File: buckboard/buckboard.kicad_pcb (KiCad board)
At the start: 2 copper layers, 171.4 x 100.4 mm, 0 parts

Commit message: Buckboard Beta 1
Ready for Ochoa review
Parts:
- added REF**: PinHeader_2x06_P2.54mm_Vertical, Connector_PinHeader_2.54mm:PinHeader_2x06_P2.54mm_Vertical, F.Cu at (213.8, 73.8)
- added REF**: MountingHole_2.2mm_M2, MountingHole:MountingHole_2.2mm_M2, F.Cu at (230.6, 72.8)
- added REF**: PinHeader_1x02_P2.54mm_Vertical, Connector_PinHeader_2.54mm:PinHeader_1x02_P2.54mm_Vertical, F.Cu at (216.3, 85.8)
- added REF**: MountingHole_2.2mm_M2, MountingHole:MountingHole_2.2mm_M2, F.Cu at (181.6, 72.8)
- added REF**: MountingHole_2.2mm_M2, MountingHole:MountingHole_2.2mm_M2, F.Cu at (174.9, 56.0)
- added REF**: PinHeader_1x02_P2.54mm_Vertical, Connector_PinHeader_2.54mm:PinHeader_1x02_P2.54mm_Vertical, F.Cu at (104.6, 103.4)
- added REF**: MountingHole_2.2mm_M2, MountingHole:MountingHole_2.2mm_M2, F.Cu at (118.9, 93.9)
- added REF**: MountingHole_2.2mm_M2, MountingHole:MountingHole_2.2mm_M2, F.Cu at (209.6, 72.8)
- added REF**: MountingHole_3.2mm_M3, MountingHole:MountingHole_3.2mm_M3, F.Cu at (231.1, 80.7)
- added REF**: MountingHole_2.2mm_M2, MountingHole:MountingHole_2.2mm_M2, F.Cu at (153.9, 72.7)
- added REF**: PinHeader_1x02_P2.54mm_Vertical, Connector_PinHeader_2.54mm:PinHeader_1x02_P2.54mm_Vertical, F.Cu at (160.6, 95.1)
- added REF**: PinHeader_2x06_P2.54mm_Vertical, Connector_PinHeader_2.54mm:PinHeader_2x06_P2.54mm_Vertical, F.Cu at (185.8, 73.8)
- added REF**: MountingHole_2.2mm_M2, MountingHole:MountingHole_2.2mm_M2, F.Cu at (202.6, 56.1)
- added REF**: MountingHole_2.2mm_M2, MountingHole:MountingHole_2.2mm_M2, F.Cu at (202.6, 72.8)
- added REF**: MountingHole_2.2mm_M2, MountingHole:MountingHole_2.2mm_M2, F.Cu at (230.6, 56.1)
- added REF**: MountingHole_2.2mm_M2, MountingHole:MountingHole_2.2mm_M2, F.Cu at (125.9, 83.4)
- added REF**: Samtec_HPM-02-01-x-S_Straight_1x02_Pitch5.08mm, Connector_Samtec_HPM_THT:Samtec_HPM-02-01-x-S_Straight_1x02_Pitch5.08mm, F.Cu at (84.1, 82.4)
- added REF**: MountingHole_2.2mm_M2, MountingHole:MountingHole_2.2mm_M2, F.Cu at (118.9, 77.2)
- added REF**: PinHeader_2x06_P2.54mm_Vertical, Connector_PinHeader_2.54mm:PinHeader_2x06_P2.54mm_Vertical, F.Cu at (102.0, 94.8)
- added REF**: PinHeader_2x06_P2.54mm_Vertical, Connector_PinHeader_2.54mm:PinHeader_2x06_P2.54mm_Vertical, F.Cu at (130.0, 84.4)
- added REF**: MountingHole_3.2mm_M3, MountingHole:MountingHole_3.2mm_M3, F.Cu at (105.5, 110.3)
- added REF**: PinHeader_2x06_P2.54mm_Vertical, Connector_PinHeader_2.54mm:PinHeader_2x06_P2.54mm_Vertical, F.Cu at (158.0, 73.6)
- added REF**: MountingHole_2.2mm_M2, MountingHole:MountingHole_2.2mm_M2, F.Cu at (146.8, 66.7)
- added REF**: PinHeader_1x02_P2.54mm_Vertical, Connector_PinHeader_2.54mm:PinHeader_1x02_P2.54mm_Vertical, F.Cu at (132.5, 100.3)
- added REF**: PinHeader_1x02_P2.54mm_Vertical, Connector_PinHeader_2.54mm:PinHeader_1x02_P2.54mm_Vertical, F.Cu at (188.3, 90.9)
- added REF**: MountingHole_3.2mm_M3, MountingHole:MountingHole_3.2mm_M3, F.Cu at (98.6, 70.8)
- added REF**: MountingHole_2.2mm_M2, MountingHole:MountingHole_2.2mm_M2, F.Cu at (146.8, 83.4)
- added REF**: MountingHole_2.2mm_M2, MountingHole:MountingHole_2.2mm_M2, F.Cu at (174.9, 72.7)
- added REF**: MountingHole_2.2mm_M2, MountingHole:MountingHole_2.2mm_M2, F.Cu at (97.9, 93.9)
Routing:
- net VIN: track 0.00 -> 211.2 mm
- net 12V1: track 0.00 -> 24.0 mm
- net 12V2: track 0.00 -> 19.6 mm
- net 9V: track 0.00 -> 18.4 mm
- net 12V3: track 0.00 -> 14.6 mm
- net 5V: track 0.00 -> 11.0 mm
- added copper zone on B.Cu, net GND
- added copper zone on F.Cu, net GND
- added copper zone on B.Cu, net VIN
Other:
- board size 171.4 x 100.4 mm -> 164.2 x 68.1 mm
- board text added: "+"
- board text added: "-"
- board text added: "12V1"
- board text added: "12V2"
- board text added: "12V3"
- board text removed: "12V(1)"
- board text removed: "12V(2)"
- board text removed: "12V(3)"
- board text removed: "3V"

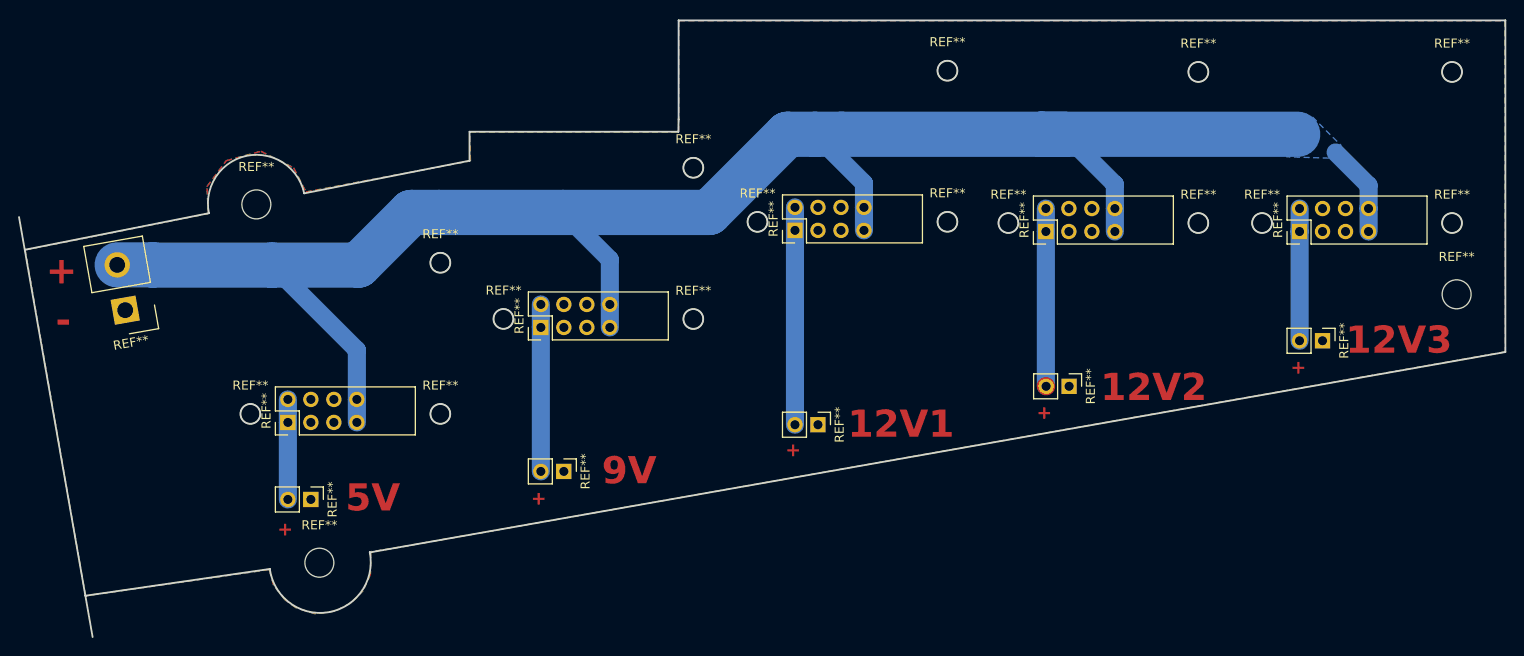
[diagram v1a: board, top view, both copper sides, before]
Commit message: Displayboard added
V1 of displayboard, this includes the SSD1309 and EC11 Rotary encoder with 1x04 JST connectors at 2.5mm pitch
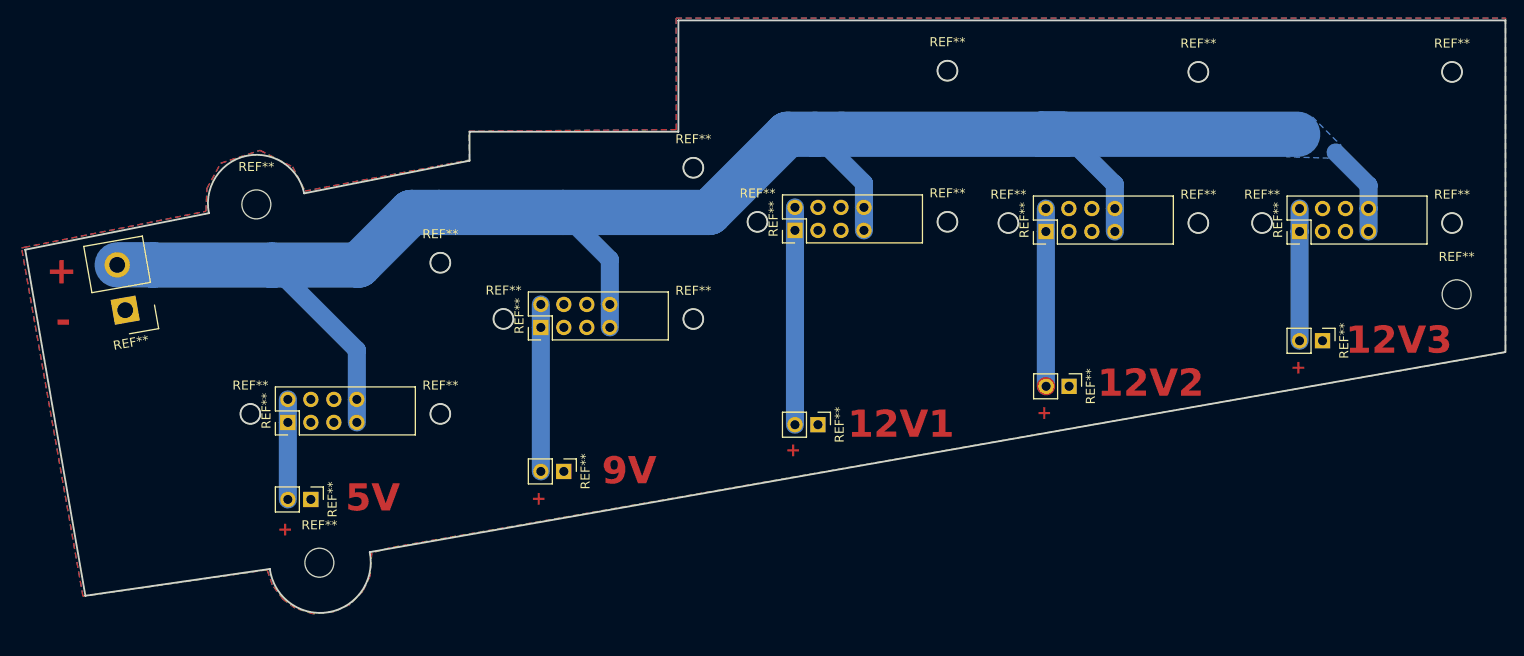
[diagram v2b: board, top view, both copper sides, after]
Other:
- board size 164.2 x 68.1 mm -> 163.5 x 65.4 mm
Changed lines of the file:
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@@
 	)
 	(setup
+		(stackup
+			(layer "F.SilkS"
+				(type "Top Silk Screen")
+			)
+			(layer "F.Paste"
+				(type "Top Solder Paste")
+			)
+			(layer "F.Mask"
+				(type "Top Solder Mask")
+				(thickness 0.01)
+			)
+			(layer "F.Cu"
+				(type "copper")
+				(thickness 0.035)
+			)
+			(layer "dielectric 1"
+				(type "core")
+				(thickness 1.51)
+				(material "FR4")
+				(epsilon_r 4.5)
+				(loss_tangent 0.02)
+			)
+			(layer "B.Cu"
+				(type "copper")
+				(thickness 0.035)
+			)
+			(layer "B.Mask"
+				(type "Bottom Solder Mask")
+				(thickness 0.01)
+			)
+			(layer "B.Paste"
+				(type "Bottom Solder Paste")
+			)
+			(layer "B.SilkS"
+				(type "Bottom Silk Screen")
+			)
+			(copper_finish "None")
+			(dielectric_constraints no)
+		)
 		(pad_to_mask_clearance 0)
 		(allow_soldermask_bridges_in_footprints no)
@@
 		(layer "Dwgs.User")
 	)
+	(gr_circle
+		(center 231.14 80.6958)
+		(end 231.7242 79.248)
+		(stroke
+			(width 0.1)
+			(type default)
+		)
+		(fill no)
+		(layer "Dwgs.User")
+	)
 	(gr_line
 		(start 198.625855 32.258)
@@
 	)
 	(gr_line
+		(start 72.9996 75.7682)
+		(end 79.6544 114.0206)
+		(stroke
+			(width 0.1)
+			(type default)
+		)
+		(layer "Dwgs.User")
+	)
+	(gr_line
 		(start 79.8576 70.779807)
 		(end 72.253308 72.120649)
@@
 		(layer "Edge.Cuts")
 	)
-	(gr_line
-		(start 80.4672 118.5418)
-		(end 72.3392 72.1614)
-		(stroke
-			(width 0.2)
-			(type default)
-		)
-		(layer "Edge.Cuts")
-	)
 	(gr_circle
 		(center 181.61 72.8218)
@@
 	)
 	(gr_line
+		(start 236.4994 87.0712)
+		(end 111.074199 109.1692)
+		(stroke
+			(width 0.2)
+			(type default)
+		)
+		(layer "Edge.Cuts")
+	)
+	(gr_line
 		(start 73.025 75.7682)
 		(end 93.310391 71.736164)
@@
 		(layer "Edge.Cuts")
 	)
+	(gr_line
+		(start 236.4994 50.4444)
+		(end 236.4994 87.0712)
+		(stroke
+			(width 0.2)
+			(type default)
+		)
+		(layer "Edge.Cuts")
+	)
 	(gr_arc
 		(start 111.0742 109.1692)
@@
 	)
 	(gr_line
-		(start 145.1864 50.4444)
-		(end 145.1864 61.3664)
-		(stroke
-			(width 0.2)
-			(type default)
-		)
-		(layer "Edge.Cuts")
-	)
-	(gr_line
 		(start 122.0978 65.9384)
 		(end 122.0978 62.738)
@@
 		(layer "Edge.Cuts")
 	)
-	(gr_line
-		(start 145.1864 50.4444)
-		(end 236.4994 50.4444)
-		(stroke
-			(width 0.2)
-			(type default)
-		)
-		(layer "Edge.Cuts")
-	)
 	(gr_circle
 		(center 230.6066 72.8218)
@@
 		(layer "Edge.Cuts")
 	)
-	(gr_circle
-		(center 174.879 56.007)
-		(end 174.1678 56.8452)
+	(gr_line
+		(start 145.161 62.738)
+		(end 145.161 50.4444)
 		(stroke
 			(width 0.2)
 			(type default)
 		)
-		(fill no)
 		(layer "Edge.Cuts")
 	)
-	(gr_line
-		(start 122.0978 62.738)
-		(end 145.161 62.738)
+	(gr_circle
+		(center 174.879 56.007)
+		(end 174.1678 56.8452)
 		(stroke
 			(width 0.2)
 			(type default)
 		)
+		(fill no)
 		(layer "Edge.Cuts")
 	)
@@
 		(layer "Edge.Cuts")
 	)
-	(gr_line
-		(start 236.4994 50.4444)
-		(end 236.4994 87.0712)
-		(stroke
-			(width 0.2)
-			(type default)
-		)
-		(layer "Edge.Cuts")
-	)
 	(gr_circle
 		(center 97.8916 93.9038)
@@
 		(layer "Edge.Cuts")
 	)
-	(gr_line
-		(start 111.08114 109.203835)
-		(end 236.4994 87.0712)
-		(stroke
-			(width 0.2)
-			(type default)
-		)
-		(layer "Edge.Cuts")
-	)
 	(gr_circle
 		(center 146.812 66.7258)
@@
 		(layer "Edge.Cuts")
 	)
+	(gr_circle
+		(center 230.6066 56.134)
+		(end 229.8954 56.9722)
+		(stroke
+			(width 0.2)
+			(type default)
+		)
+		(fill no)
+		(layer "Edge.Cuts")
+	)
 	(gr_line
-		(start 145.161 62.738)
-		(end 145.1864 61.3664)
+		(start 79.669096 113.98762)
+		(end 73.025 75.7682)
 		(stroke
 			(width 0.2)
@@
 		(layer "Edge.Cuts")
 	)
-	(gr_circle
-		(center 230.6066 56.134)
-		(end 229.8954 56.9722)
+	(gr_line
+		(start 122.0978 62.738)
+		(end 145.161 62.738)
 		(stroke
 			(width 0.2)
 			(type default)
 		)
-		(fill no)
 		(layer "Edge.Cuts")
 	)
@@
 		(layer "Edge.Cuts")
 	)
+	(gr_line
+		(start 145.161 50.4444)
+		(end 236.4994 50.4444)
+		(stroke
+			(width 0.2)
+			(type default)
+		)
+		(layer "Edge.Cuts")
+	)
 	(gr_text "12V1"
 		(at 163.8554 96.7994 0)
@@
 	)
 	(gr_text "12V2"
-		(at 191.77 92.7354 0)
+		(at 191.4398 92.2528 0)
 		(layer "F.Cu")
 		(effects
@@
 		(polygon
 			(pts
-				(xy 73.025 75.7936) (xy 93.2434 71.7804) (xy 93.091 68.8086) (xy 95.2246 65.9384) (xy 99.06 64.897)
-				(xy 102.6668 66.7258) (xy 104.0384 69.3928) (xy 122.1994 65.9638) (xy 122.1232 62.7888) (xy 145.1864 62.7888)
-				(xy 145.2118 50.4698) (xy 236.4486 50.4698) (xy 236.4994 87.0458) (xy 113.4364 108.7882) (xy 111.2012 109.1184)
-				(xy 111.1504 111.633) (xy 110.3376 113.4364) (xy 109.0168 114.7826) (xy 107.2134 115.697) (xy 105.029 115.9764)
-				(xy 102.9716 115.3414) (xy 101.7016 114.427) (xy 100.457 112.8268) (xy 99.9744 111.0996) (xy 79.6798 113.9952)
-				(xy 73.025 75.8444)
+				(xy 72.9234 75.5142) (xy 92.9894 71.5264) (xy 93.091 69.0118) (xy 94.615 66.2178) (xy 98.9584 64.7954)
+				(xy 102.5652 66.6242) (xy 103.9368 69.2912) (xy 122.0978 65.8622) (xy 122.0216 62.6872) (xy 144.9324 62.5094)
+				(xy 144.907 50.1904) (xy 236.5248 50.1904) (xy 236.5248 87.0966) (xy 113.3348 108.6866) (xy 111.3028 109.2454)
+				(xy 111.0996 111.8362) (xy 110.3122 113.4872) (xy 108.9152 114.935) (xy 107.1372 115.7478) (xy 104.8004 115.9764)
+				(xy 102.8192 115.3414) (xy 101.4984 114.3762) (xy 100.3046 112.776) (xy 99.7458 111.125) (xy 79.4004 114.046)
+				(xy 72.6186 75.565)
 			)
 		)
@@
 		)
 	)
+	(group ""
+		(members "08ac290c-cd75-446d-a283-69a62430721d" "100f6bb0-8ac1-4aa8-8df4-68425ee58a96"
+			"14fcc44f-f9c8-4de5-a443-d8060994849b" "19a24748-5a23-4def-b4ac-534d46091593"
+			"1f5220b4-85c4-4825-9cb8-5540edd776f1" "29a9c7e6-edba-41b2-88ba-42d74fc42518"
+			"3b85ee02-43b3-49b5-8263-29d65321620f" "3e021f75-e3d1-466f-a82d-592c27f220af"
+			"487a05c4-4d65-4580-81c5-162e8570d186" "492f5762-d367-4f8f-89e6-e75369b99074"
+			"522a5daa-b4cc-4f55-8a43-47368492fb03" "53abff7b-cace-44b8-a80f-b22d5f4d4c50"
+			"54f060bc-0780-4725-9e6f-3ea997aea16f" "69adb5fd-d910-45b1-b241-f7b099c2820d"
+			"6adc377e-e88e-4b54-bdba-fac3ffd49ba0" "6e200bb5-f3e1-41d2-8d77-5c1d2503f099"
+			"728d0a3e-a5f4-4685-bcae-40d5e5fbf530" "74165322-ee42-419d-bd47-88f6423765a2"
+			"753f1005-65d1-4fc4-b77d-4bd882c4ae62" "7c9931a1-2599-4b11-be92-e460cc33d30c"
+			"7e308f98-fb6c-45fa-b5be-21807d6c1e51" "803e3df1-39b3-4b50-9648-588f74422d63"
+			"86e9b90d-82b7-4cb8-b2d2-05c636e7abfc" "8ab7ee58-7a19-4eaf-a512-e4e011e104a4"
+			"9a4d98c8-8188-4a34-ba1d-e7185f168cd8" "9fdf1d90-d9f6-4e2e-80a1-ef531dc6205f"
+			"a3b4a6e2-f054-4eb3-8551-e894acd52332" "a4385cd8-49ca-4996-aca1-30fc9fb4e0fb"
+			"ad450666-beea-4056-aa28-05f9b408d53b" "ae7e8b20-3739-4d6c-80e1-d8a6fa7bc08d"
+			"ba623425-5180-43ef-b5dc-61c3fc3b580d" "c939d797-44a2-47a3-ba63-0be7c99642f2"
+			"cc096376-f6ec-4625-a543-b02c33cafc7a" "d3aad463-800c-471e-8e0a-56622d526e9b"
+			"d5f47c33-46c5-4eef-8c19-71c94d36bad1" "d92017c2-8270-4b24-a4d1-3dc9bd8df992"
+			"ddb90e7e-b805-409e-8145-4f357c224431" "e011034f-33a2-48b9-9f87-4f56acfee713"
+			"e35176ff-c8aa-4430-be5a-05ac66e4ad7f" "e3cce3ca-6085-4f91-810d-08f08806099e"
+			"e6b83a4e-7aae-4d3d-bdc8-64fd230ead2f" "e8bd8532-d39e-4069-8c25-a64634412c35"
+			"ed3d3a9c-fba3-4353-831f-3840b9a1c39f" "ff6776fd-2066-4b64-a103-c9d81213c82c"
+		)
+	)

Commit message: V1.2
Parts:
- removed the REF** at (146.8, 66.7)
- added REF**: Fuseholder_Cylinder-5x20mm_Schurter_0031_8201_Horizontal_Op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, Fuse:Fuseholder_Cylinder-5x20mm_Schurter_0031_8201_Horizontal_Open, F.Cu at (125.7, 87.8)
- added REF**: Fuseholder_Cylinder-5x20mm_Schurter_0031_8201_Horizontal_Op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, Fuse:Fuseholder_Cylinder-5x20mm_Schurter_0031_8201_Horizontal_Open, F.Cu at (106.9, 87.7)
- added REF**: Fuseholder_Cylinder-5x20mm_Schurter_0031_8201_Horizontal_Op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, Fuse:Fuseholder_Cylinder-5x20mm_Schurter_0031_8201_Horizontal_Open, F.Cu at (175.0, 78.6)
- added REF**: PinHeader_2x06_P2.54mm_Vertical, Connector_PinHeader_2.54mm:PinHeader_2x06_P2.54mm_Vertical, F.Cu at (158.1, 108.7)
- added REF**: PinHeader_1x02_P2.54mm_Vertical, Connector_PinHeader_2.54mm:PinHeader_1x02_P2.54mm_Vertical, F.Cu at (160.8, 113.5)
- added REF**: MountingHole_2.2mm_M2, MountingHole:MountingHole_2.2mm_M2, F.Cu at (175.0, 107.9)
- added REF**: Fuseholder_Cylinder-5x20mm_Schurter_0031_8201_Horizontal_Op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, Fuse:Fuseholder_Cylinder-5x20mm_Schurter_0031_8201_Horizontal_Open, F.Cu at (174.7, 37.5)
- added REF**: MountingHole_2.2mm_M2, MountingHole:MountingHole_2.2mm_M2, F.Cu at (153.9, 107.9)
- added REF**: Fuseholder_Cylinder-5x20mm_Schurter_0031_8201_Horizontal_Op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, Fuse:Fuseholder_Cylinder-5x20mm_Schurter_0031_8201_Horizontal_Open, F.Cu at (193.7, 68.6)
- added REF**: Fuseholder_Cylinder-5x20mm_Schurter_0031_8201_Horizontal_Op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, Fuse:Fuseholder_Cylinder-5x20mm_Schurter_0031_8201_Horizontal_Open, F.Cu at (183.0, 61.8)
- added REF**: MountingHole_2.2mm_M2, MountingHole:MountingHole_2.2mm_M2, F.Cu at (175.0, 86.8)
- moved REF** 61.8 mm to (184.0, 66.1)
- moved REF** 59.1 mm to (113.8, 116.2)
- moved REF** 59.1 mm to (134.9, 116.2)
- moved REF** 59.1 mm to (118.0, 117.0)
- moved REF** 55.9 mm to (134.9, 95.1)
- moved REF** 47.6 mm to (120.6, 121.0)
- moved REF** 32.6 mm to (175.0, 67.1)
- moved REF** 32.6 mm to (158.1, 68.0)
- moved REF** 32.5 mm to (153.9, 67.1)
- moved REF** 29.8 mm to (84.6, 120.5)
- moved REF** 29.7 mm to (105.6, 120.5)
- moved REF** 29.7 mm to (88.8, 121.4)
- moved REF** 26.0 mm to (91.3, 125.6)
- moved REF** 26.0 mm to (105.6, 99.5)
- moved REF** 21.1 mm to (203.1, 93.9)
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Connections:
- net 12V1 renamed 5V2
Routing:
- net VIN: track 211.2 -> 389.3 mm, vias 0 -> 2
- net 5V2: track 24.0 -> 6.53 mm
- net 9V: track 18.4 -> 32.6 mm
- net 12V1: track 0.00 -> 7.37 mm
- net 12V3: track 14.6 -> 10.2 mm
- net 12V2: track 19.6 -> 15.3 mm
- net 5V: track 11.0 -> 6.76 mm
- removed copper zone on B.Cu, net VIN
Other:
- board size 163.5 x 65.4 mm -> 164.1 x 99.4 mm
- board text added: "5V1"
- board text added: "5V2"
- board text removed: "5V"
